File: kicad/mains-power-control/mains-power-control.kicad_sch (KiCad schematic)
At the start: 25 parts, among them J1 Conn_01x04_Socket, J2 Conn_01x06_Pin, J3 Conn_01x03_Pin, J4 Conn_01x03_Pin, J7 Conn_01x03_Pin, J9 Conn_01x03_Pin, Q1 ZVN4206AV, U1 BP, U2 SeeeduinoXIAO, U3 MOC3020M, U5 H11AA1

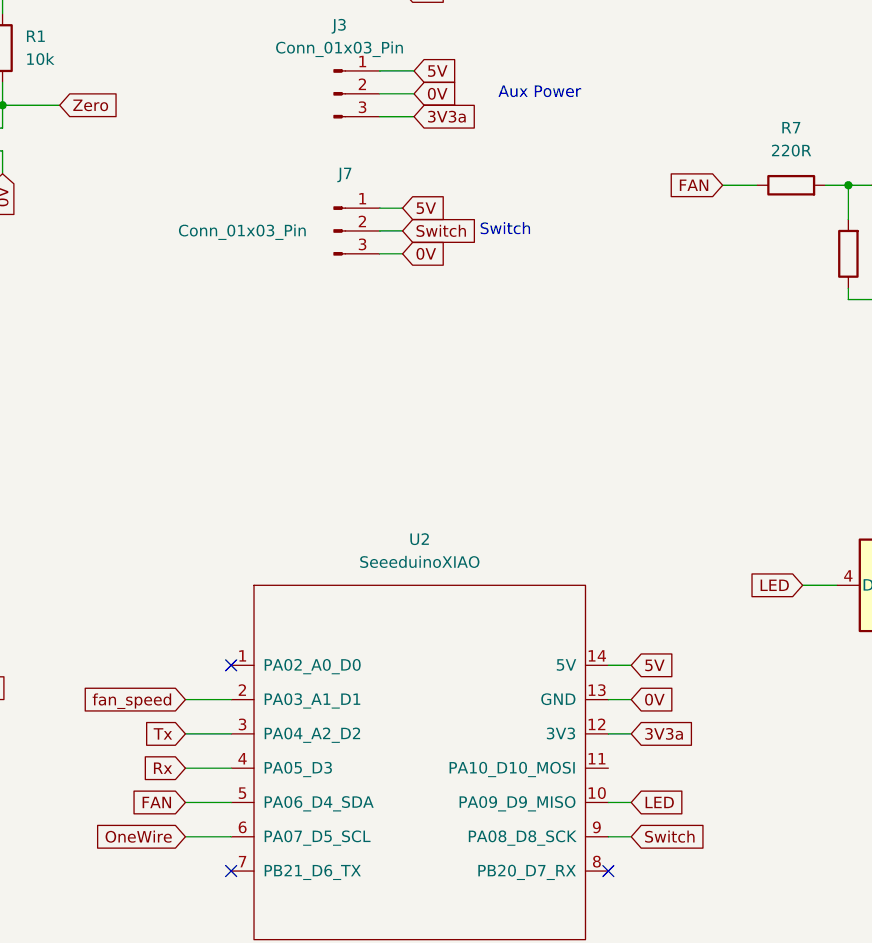
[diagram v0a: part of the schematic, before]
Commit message: Added 'lamp' signal to driver power indicator
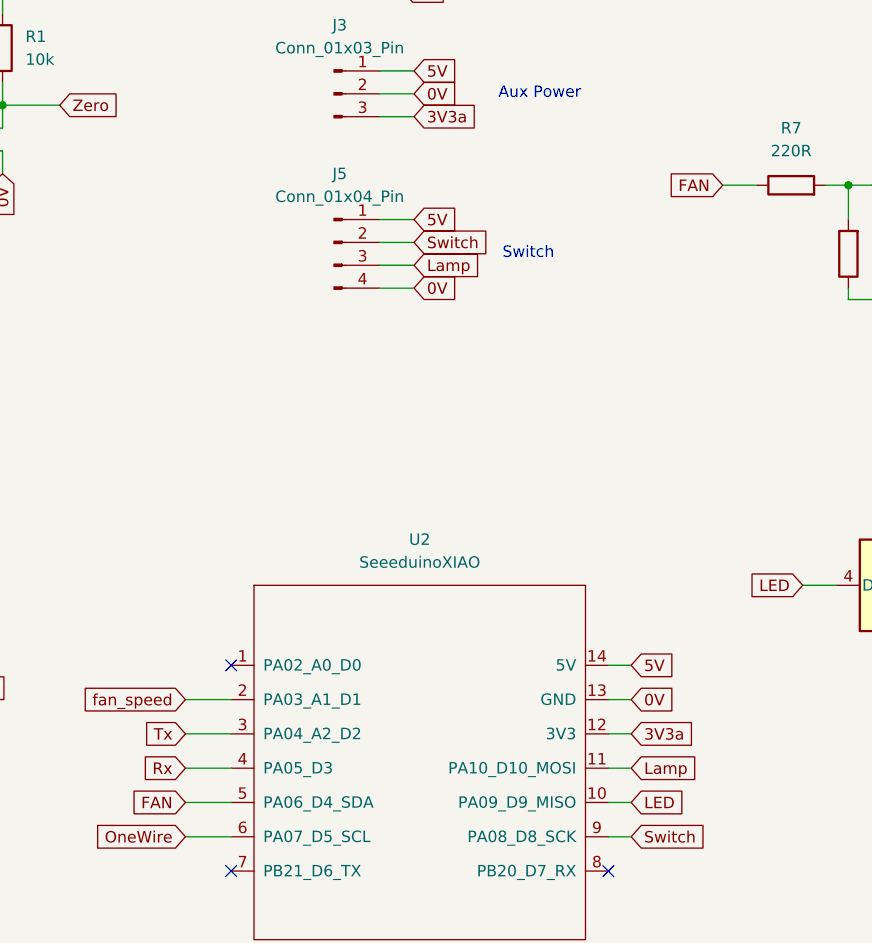
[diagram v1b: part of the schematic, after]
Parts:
- removed J7: Conn_01x03_Pin, Connector_PinHeader_2.54mm:PinHeader_1x03_P2.54mm_Vertical, symbol Connector:Conn_01x03_Pin
- added J5: Conn_01x04_Pin, Connector_PinHeader_2.54mm:PinHeader_1x04_P2.54mm_Vertical, symbol Connector:Conn_01x04_Pin
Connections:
- net 0V: now also J5.4 (Pin_4)
- net 5V: now also J5.1 (Pin_1)
- net Switch: now also J5.2 (Pin_2)
- net Lamp: now reaches U2.11 (PA10_D10_MOSI)
- net Lamp: now also J5.3 (Pin_3)
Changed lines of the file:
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@@
 	(text "Switch"
 		(exclude_from_sim no)
-		(at 181.61 62.23 0)
+		(at 184.15 64.77 0)
 		(effects
 			(font
@@
 	(wire
 		(pts
-			(xy 167.64 62.23) (xy 170.18 62.23)
+			(xy 76.2 113.03) (xy 78.74 113.03)
 		)
 		(stroke
@@
 	(wire
 		(pts
-			(xy 76.2 113.03) (xy 78.74 113.03)
+			(xy 193.04 114.3) (xy 195.58 114.3)
 		)
 		(stroke
@@
 	(wire
 		(pts
-			(xy 193.04 114.3) (xy 195.58 114.3)
+			(xy 167.64 44.45) (xy 171.45 44.45)
 		)
 		(stroke
@@
 	(wire
 		(pts
-			(xy 167.64 44.45) (xy 171.45 44.45)
+			(xy 226.06 109.22) (xy 226.06 113.03)
 		)
 		(stroke
@@
 	(wire
 		(pts
-			(xy 226.06 109.22) (xy 226.06 113.03)
+			(xy 67.31 73.66) (xy 69.85 73.66)
 		)
 		(stroke
@@
 	(wire
 		(pts
-			(xy 67.31 73.66) (xy 69.85 73.66)
+			(xy 90.17 48.26) (xy 93.98 48.26)
 		)
 		(stroke
@@
 	(wire
 		(pts
-			(xy 90.17 48.26) (xy 93.98 48.26)
+			(xy 167.64 66.04) (xy 171.45 66.04)
 		)
 		(stroke
@@
 	(wire
 		(pts
+			(xy 167.64 68.58) (xy 171.45 68.58)
+		)
+		(stroke
+			(width 0)
+			(type default)
+		)
+	)
+	(wire
+		(pts
+			(xy 167.64 60.96) (xy 171.45 60.96)
+		)
+		(stroke
+			(width 0)
+			(type default)
+		)
+	)
+	(wire
+		(pts
 			(xy 39.37 73.66) (xy 41.91 73.66)
 		)
@@
 	(wire
 		(pts
-			(xy 167.64 64.77) (xy 170.18 64.77)
+			(xy 234.95 39.37) (xy 241.3 39.37)
 		)
 		(stroke
@@
 	(wire
 		(pts
-			(xy 234.95 39.37) (xy 241.3 39.37)
+			(xy 237.49 69.85) (xy 237.49 72.39)
 		)
 		(stroke
@@
 	(wire
 		(pts
-			(xy 237.49 69.85) (xy 237.49 72.39)
+			(xy 90.17 53.34) (xy 105.41 53.34)
 		)
 		(stroke
@@
 	(wire
 		(pts
-			(xy 90.17 53.34) (xy 105.41 53.34)
+			(xy 167.64 30.48) (xy 170.18 30.48)
 		)
 		(stroke
@@
 	(wire
 		(pts
-			(xy 167.64 30.48) (xy 170.18 30.48)
+			(xy 234.95 49.53) (xy 234.95 50.8)
 		)
 		(stroke
@@
 	(wire
 		(pts
-			(xy 234.95 49.53) (xy 234.95 50.8)
+			(xy 101.6 152.4) (xy 101.6 154.94)
 		)
 		(stroke
@@
 	(wire
 		(pts
-			(xy 167.64 59.69) (xy 170.18 59.69)
+			(xy 57.15 78.74) (xy 59.69 78.74)
 		)
 		(stroke
@@
 	(wire
 		(pts
-			(xy 101.6 152.4) (xy 101.6 154.94)
+			(xy 146.05 114.3) (xy 151.13 114.3)
 		)
 		(stroke
@@
 	(wire
 		(pts
-			(xy 57.15 78.74) (xy 59.69 78.74)
+			(xy 205.74 57.15) (xy 209.55 57.15)
 		)
 		(stroke
@@
 	(wire
 		(pts
-			(xy 146.05 114.3) (xy 151.13 114.3)
+			(xy 116.84 133.35) (xy 119.38 133.35)
 		)
 		(stroke
@@
 	(wire
 		(pts
-			(xy 205.74 57.15) (xy 209.55 57.15)
+			(xy 57.15 73.66) (xy 59.69 73.66)
 		)
 		(stroke
@@
 	(wire
 		(pts
-			(xy 116.84 133.35) (xy 119.38 133.35)
+			(xy 193.04 121.92) (xy 195.58 121.92)
 		)
 		(stroke
@@
 	(wire
 		(pts
-			(xy 57.15 73.66) (xy 59.69 73.66)
+			(xy 167.64 63.5) (xy 171.45 63.5)
 		)
 		(stroke
@@
 	(global_label "5V"
 		(shape input)
-		(at 170.18 59.69 0)
+		(at 171.45 60.96 0)
 		(fields_autoplaced yes)
 		(effects
@@
 		)
 		(property "Intersheetrefs" "${INTERSHEET_REFS}"
-			(at 175.4633 59.69 0)
+			(at 176.7333 60.96 0)
 			(effects
 				(font
@@
 		)
 	)
+	(global_label "Lamp"
+		(shape input)
+		(at 171.45 66.04 0)
+		(fields_autoplaced yes)
+		(effects
+			(font
+				(size 1.27 1.27)
+			)
+			(justify left)
+		)
+		(property "Intersheetrefs" "${INTERSHEET_REFS}"
+			(at 179.4546 66.04 0)
+			(effects
+				(font
+					(size 1.27 1.27)
+				)
+				(justify left)
+				(hide yes)
+			)
+		)
+	)
 	(global_label "Rx"
 		(shape input)
@@
 	(global_label "Switch"
 		(shape input)
-		(at 170.18 62.23 0)
+		(at 171.45 63.5 0)
 		(fields_autoplaced yes)
 		(effects
@@
 		)
 		(property "Intersheetrefs" "${INTERSHEET_REFS}"
-			(at 179.2733 62.23 0)
+			(at 180.5433 63.5 0)
 			(effects
 				(font
@@
 		)
 	)
+	(global_label "Lamp"
+		(shape input)
+		(at 195.58 121.92 0)
+		(fields_autoplaced yes)
+		(effects
+			(font
+				(size 1.27 1.27)
+			)
+			(justify left)
+		)
+		(property "Intersheetrefs" "${INTERSHEET_REFS}"
+			(at 203.5846 121.92 0)
+			(effects
+				(font
+					(size 1.27 1.27)
+				)
+				(justify left)
+				(hide yes)
+			)
+		)
+	)
 	(global_label "Zero"
 		(shape input)
@@
 	(global_label "0V"
 		(shape input)
-		(at 170.18 64.77 0)
+		(at 171.45 68.58 0)
 		(fields_autoplaced yes)
 		(effects
@@
 		)
 		(property "Intersheetrefs" "${INTERSHEET_REFS}"
-			(at 175.4633 64.77 0)
+			(at 176.7333 68.58 0)
 			(effects
 				(font
@@
 	)
 	(symbol
+		(lib_id "Connector:Conn_01x04_Pin")
+		(at 162.56 63.5 0)
+		(unit 1)
+		(exclude_from_sim no)
+		(in_bom yes)
+		(on_board yes)
+		(dnp no)
+		(fields_autoplaced yes)
+		(property "Reference" "J5"
+			(at 163.195 55.88 0)
+			(effects
+				(font
+					(size 1.27 1.27)
+				)
+			)
+		)
+		(property "Value" "Conn_01x04_Pin"
+			(at 163.195 58.42 0)
+			(effects
+				(font
+					(size 1.27 1.27)
+				)
+			)
+		)
+		(property "Footprint" "Connector_PinHeader_2.54mm:PinHeader_1x04_P2.54mm_Vertical"
+			(at 162.56 63.5 0)
+			(effects
+				(font
+					(size 1.27 1.27)
+				)
+				(hide yes)
+			)
+		)
+		(property "Datasheet" "~"
+			(at 162.56 63.5 0)
+			(effects
+				(font
+					(size 1.27 1.27)
+				)
+				(hide yes)
+			)
+		)
+		(property "Description" "Generic connector, single row, 01x04, script generated"
+			(at 162.56 63.5 0)
+			(effects
+				(font
+					(size 1.27 1.27)
+				)
+				(hide yes)
+			)
+		)
+		(pin "4"
+		)
+		(pin "1"
+		)
+		(pin "3"
+		)
+		(pin "2"
+		)
+		(instances
+			(project ""
+				(path "/ef5d369c-2cce-4e32-8236-63587eb624d9"
+					(reference "J5")
+					(unit 1)
+				)
+			)
+		)
+	)
+	(symbol
 		(lib_id "Connector:Conn_01x06_Pin")
 		(at 34.29 102.87 0)
@@
 					(unit 1)
 				)
-			)
-		)
-	)
-	(symbol
-		(lib_id "Connector:Conn_01x03_Pin")
-		(at 162.56 62.23 0)
-		(unit 1)
-		(exclude_from_sim no)
-		(in_bom yes)
-		(on_board yes)
-		(dnp no)
-		(property "Reference" "J7"
-			(at 163.83 55.88 0)
-			(effects
-				(font
-					(size 1.27 1.27)
-				)
-			)
-		)
-		(property "Value" "Conn_01x03_Pin"
-			(at 152.4 62.23 0)
-			(effects
-				(font
-					(size 1.27 1.27)
-				)
-			)
-		)
-		(property "Footprint" "Connector_PinHeader_2.54mm:PinHeader_1x03_P2.54mm_Vertical"
-			(at 162.56 62.23 0)
-			(effects
-				(font
-					(size 1.27 1.27)
-				)
-				(hide yes)
-			)
-		)
-		(property "Datasheet" "~"
-			(at 162.56 62.23 0)
-			(effects
-				(font
-					(size 1.27 1.27)
-				)
-				(hide yes)
-			)
-		)
-		(property "Description" "Generic connector, single row, 01x03, script generated"
-			(at 162.56 62.23 0)
-			(effects
-				(font
-					(size 1.27 1.27)
-				)
-				(hide yes)
-			)
-		)
-		(pin "3"
-		)
-		(pin "2"
-		)
-		(pin "1"
-		)
-		(instances
-			(project "mains-power-control"
-				(path "/ef5d369c-2cce-4e32-8236-63587eb624d9"
-					(reference "J7")
-					(unit 1)
-				)

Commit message: PCB v 1.1
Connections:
- net 0V: now also J5.3 (Pin_3); no longer J5.4 (Pin_4)
- net Lamp: now also J5.4 (Pin_4); no longer J5.3 (Pin_3)
